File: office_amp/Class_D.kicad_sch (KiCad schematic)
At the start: 51 parts, among them J7 Screw_Terminal_01x04, Q6 BC856, Q7 BC850, Q8 BC856, Q9 BC856, U10 DS1882E, U12 TL082, U6 TPA3123D2

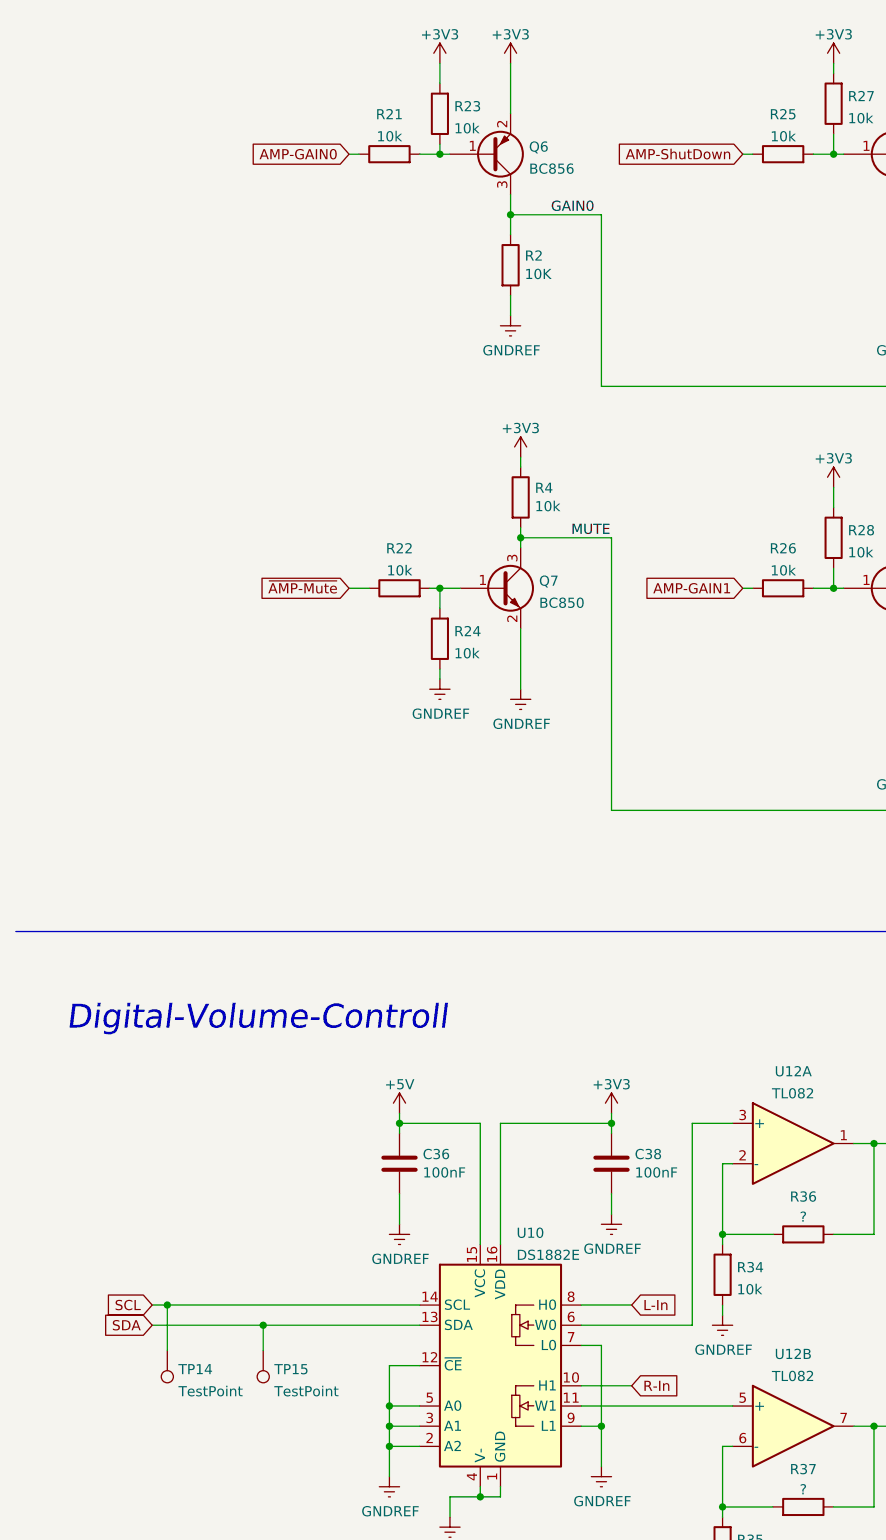
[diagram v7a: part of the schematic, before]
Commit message: Organized Schematic
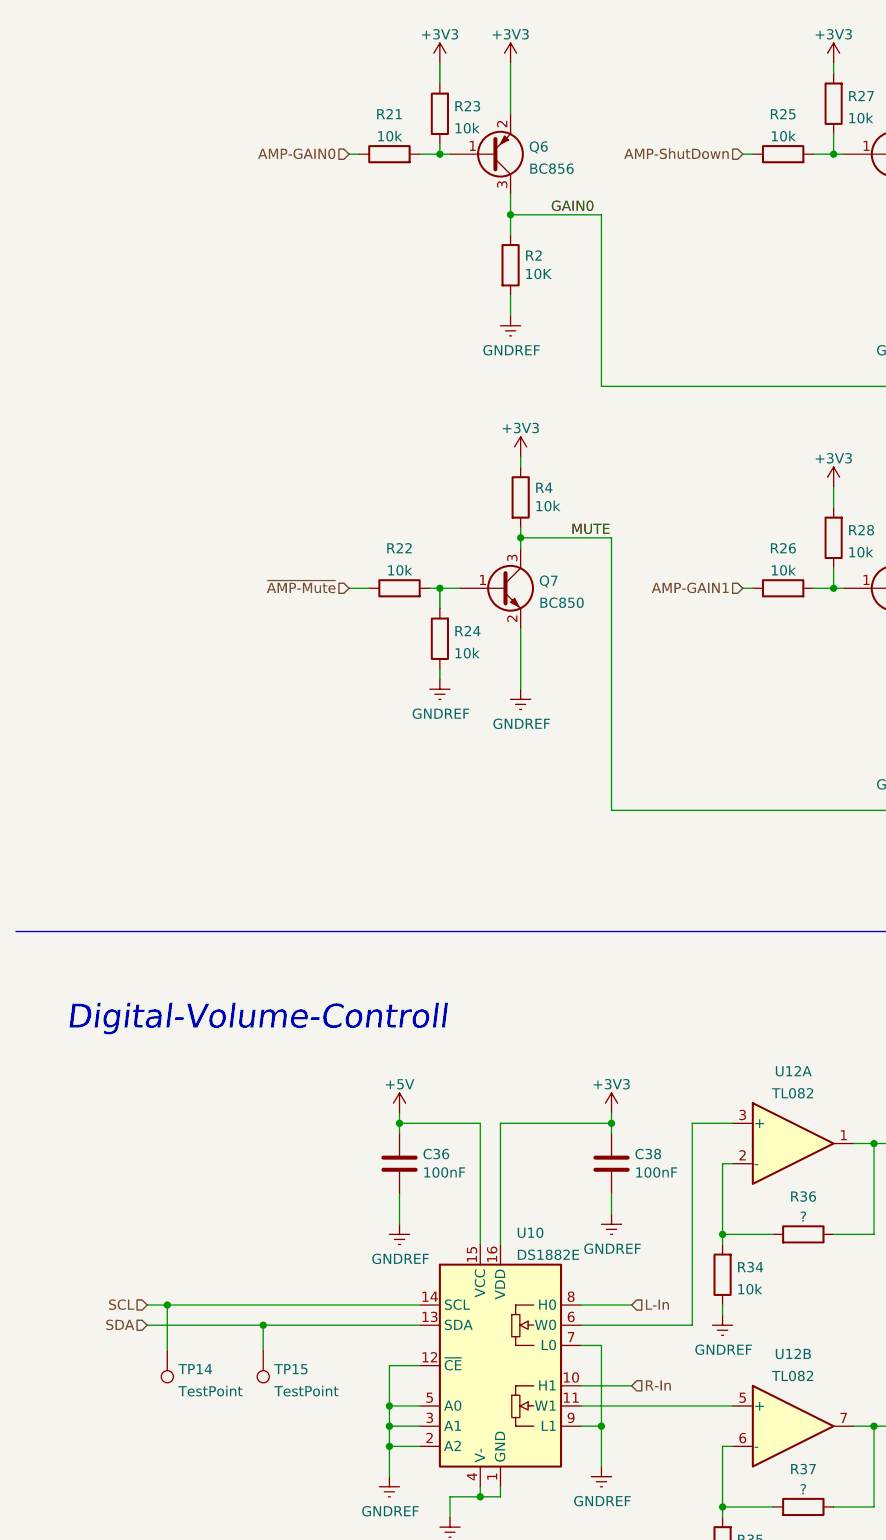
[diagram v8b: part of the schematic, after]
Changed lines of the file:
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@@
     (stroke (width 0) (type default) (color 0 0 0 0))
   )
-  (wire (pts (xy 29.845 186.69) (xy 31.75 186.69))
+  (wire (pts (xy 29.21 186.69) (xy 31.75 186.69))
     (stroke (width 0) (type default) (color 0 0 0 0))
   )
@@
     (stroke (width 0) (type default) (color 0 0 0 0))
   )
-  (wire (pts (xy 29.845 189.23) (xy 43.815 189.23))
+  (wire (pts (xy 29.21 189.23) (xy 43.815 189.23))
     (stroke (width 0) (type default) (color 0 0 0 0))
   )
@@
     (effects (font (size 1.27 1.27)) (justify left bottom))
   )
-  (global_label "~{AMP-Mute}" (shape input) (at 54.61 96.52 180) (fields_autoplaced)
+  (hierarchical_label "AMP-GAIN0" (shape input) (at 54.61 41.91 180)
     (effects (font (size 1.27 1.27)) (justify right))
-    (property "Intersheet References" "${INTERSHEET_REFS}" (id 0) (at 42.4887 96.4406 0)
-      (effects (font (size 1.27 1.27)) (justify right) hide)
-    )
-  )
-  (global_label "AMP-GAIN1" (shape input) (at 104.14 96.52 180) (fields_autoplaced)
+  )
+  (hierarchical_label "AMP-GAIN1" (shape input) (at 104.14 96.52 180)
     (effects (font (size 1.27 1.27)) (justify right))
-    (property "Intersheet References" "${INTERSHEET_REFS}" (id 0) (at 90.9301 96.4406 0)
-      (effects (font (size 1.27 1.27)) (justify right) hide)
-    )
-  )
-  (global_label "AMP-ShutDown" (shape input) (at 104.14 41.91 180) (fields_autoplaced)
+  )
+  (hierarchical_label "L-In" (shape input) (at 90.17 186.69 0)
+    (effects (font (size 1.27 1.27)) (justify left))
+  )
+  (hierarchical_label "AMP-ShutDown" (shape input) (at 104.14 41.91 180)
     (effects (font (size 1.27 1.27)) (justify right))
-    (property "Intersheet References" "${INTERSHEET_REFS}" (id 0) (at 87.3015 41.8306 0)
-      (effects (font (size 1.27 1.27)) (justify right) hide)
-    )
-  )
-  (global_label "AMP-GAIN0" (shape input) (at 54.61 41.91 180) (fields_autoplaced)
+  )
+  (hierarchical_label "R-In" (shape input) (at 90.17 196.85 0)
+    (effects (font (size 1.27 1.27)) (justify left))
+  )
+  (hierarchical_label "~{AMP-Mute}" (shape input) (at 54.61 96.52 180)
     (effects (font (size 1.27 1.27)) (justify right))
-    (property "Intersheet References" "${INTERSHEET_REFS}" (id 0) (at 41.4001 41.8306 0)
-      (effects (font (size 1.27 1.27)) (justify right) hide)
-    )
-  )
-  (global_label "SDA" (shape input) (at 29.845 189.23 180) (fields_autoplaced)
+  )
+  (hierarchical_label "SCL" (shape input) (at 29.21 186.69 180)
     (effects (font (size 1.27 1.27)) (justify right))
-    (property "Intersheet References" "${INTERSHEET_REFS}" (id 0) (at 23.9527 189.1506 0)
-      (effects (font (size 1.27 1.27)) (justify right) hide)
-    )
-  )
-  (global_label "R-In" (shape input) (at 90.17 196.85 0) (fields_autoplaced)
-    (effects (font (size 1.27 1.27)) (justify left))
-    (property "Intersheet References" "${INTERSHEET_REFS}" (id 0) (at 146.05 364.49 0)
-      (effects (font (size 1.27 1.27)) hide)
-    )
-  )
-  (global_label "L-In" (shape input) (at 90.17 186.69 0) (fields_autoplaced)
-    (effects (font (size 1.27 1.27)) (justify left))
-    (property "Intersheet References" "${INTERSHEET_REFS}" (id 0) (at 146.05 341.63 0)
-      (effects (font (size 1.27 1.27)) hide)
-    )
-  )
-  (global_label "SCL" (shape input) (at 29.845 186.69 180) (fields_autoplaced)
+  )
+  (hierarchical_label "SDA" (shape input) (at 29.21 189.23 180)
     (effects (font (size 1.27 1.27)) (justify right))
-    (property "Intersheet References" "${INTERSHEET_REFS}" (id 0) (at 24.0132 186.6106 0)
-      (effects (font (size 1.27 1.27)) (justify right) hide)
-    )
   )
   (symbol (lib_id "OfficeAmp:TPA3123D2") (at 226.06 87.63 0) (unit 1)
